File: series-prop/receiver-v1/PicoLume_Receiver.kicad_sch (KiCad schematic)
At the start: 67 parts, among them IC1 LM66200DRLR, J1 Conn_01x17, J10 Conn_01x03_Pin, J11 Conn_01x04_Pin, J13 USB_C_Receptacle_USB2.0_16P, J2 Conn_01x04_Pin, J4 Conn_01x17, J5 Conn_01x01_Pin, J6 Screw_Terminal_01x02, J7 Screw_Terminal_01x03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

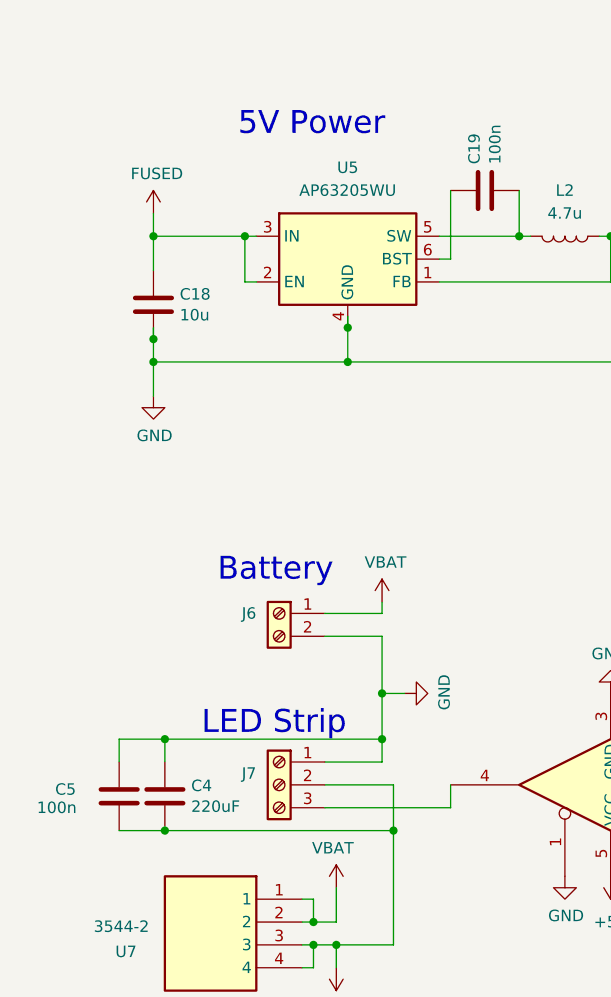
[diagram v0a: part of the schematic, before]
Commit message: Removed bulk output cap and added PTC on VBAT input
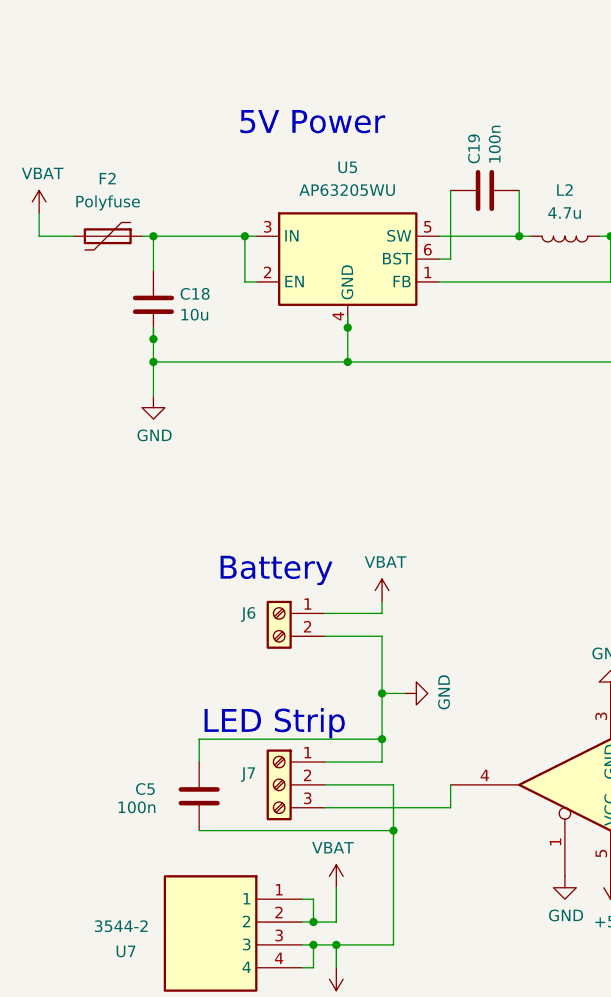
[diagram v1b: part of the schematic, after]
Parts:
- removed C4: 220uF, Capacitor_SMD:CP_Elec_8x10, symbol Device:C
- added F2: Polyfuse, Fuse:Fuse_1210_3225Metric, symbol Device:Polyfuse
- F1: footprint Fuse:Fuse_1206_3216Metric -> Fuse:Fuse_1210_3225Metric; LCSC C207036 -> C20617440
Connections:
- net FUSED: no longer C18.1, U5.2 (EN), U5.3 (IN)
- net VBAT: now also F2.2
- new net: C18.1, F2.1, U5.2 (EN), U5.3 (IN)
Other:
- moved on the sheet: C5
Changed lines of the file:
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@@
 	)
 	(junction
-		(at 49.53 177.8)
-		(diameter 0)
-		(color 0 0 0 0)
-	)
-	(junction
 		(at 88.9 111.76)
 		(diameter 0)
@@
 	)
 	(junction
-		(at 49.53 167.64)
-		(diameter 0)
-		(color 0 0 0 0)
-	)
-	(junction
 		(at 69.85 125.73)
 		(diameter 0)
@@
 	)
 	(junction
+		(at 48.26 111.76)
+		(diameter 0)
+		(color 0 0 0 0)
+	)
+	(junction
 		(at 73.66 59.69)
 		(diameter 0)
@@
 	)
 	(junction
-		(at 48.26 111.76)
-		(diameter 0)
-		(color 0 0 0 0)
-	)
-	(junction
 		(at 74.93 39.37)
 		(diameter 0)
@@
 	(wire
 		(pts
-			(xy 44.45 177.8) (xy 49.53 177.8)
-		)
-		(stroke
-			(width 0)
-			(type default)
-		)
-	)
-	(wire
-		(pts
 			(xy 201.93 109.22) (xy 201.93 114.3)
 		)
@@
 	(wire
 		(pts
+			(xy 35.56 111.76) (xy 39.37 111.76)
+		)
+		(stroke
+			(width 0)
+			(type default)
+		)
+	)
+	(wire
+		(pts
 			(xy 213.36 109.22) (xy 247.65 109.22)
 		)
@@
 	(wire
 		(pts
-			(xy 49.53 167.64) (xy 73.66 167.64)
+			(xy 53.34 167.64) (xy 73.66 167.64)
 		)
 		(stroke
@@
 	(wire
 		(pts
-			(xy 49.53 177.8) (xy 74.93 177.8)
+			(xy 53.34 177.8) (xy 74.93 177.8)
 		)
 		(stroke
@@
 	(wire
 		(pts
+			(xy 46.99 111.76) (xy 48.26 111.76)
+		)
+		(stroke
+			(width 0)
+			(type default)
+		)
+	)
+	(wire
+		(pts
 			(xy 373.38 36.83) (xy 387.35 36.83)
 		)
@@
 	(wire
 		(pts
-			(xy 49.53 167.64) (xy 49.53 170.18)
-		)
-		(stroke
-			(width 0)
-			(type default)
-		)
-	)
-	(wire
-		(pts
 			(xy 236.22 49.53) (xy 233.68 49.53)
 		)
@@
 	(wire
 		(pts
-			(xy 44.45 167.64) (xy 49.53 167.64)
-		)
-		(stroke
-			(width 0)
-			(type default)
-		)
-	)
-	(wire
-		(pts
 			(xy 279.4 105.41) (xy 290.83 105.41)
 		)
@@
 	(wire
 		(pts
+			(xy 35.56 109.22) (xy 35.56 111.76)
+		)
+		(stroke
+			(width 0)
+			(type default)
+		)
+	)
+	(wire
+		(pts
 			(xy 373.38 105.41) (xy 379.73 105.41)
 		)
@@
 	(wire
 		(pts
-			(xy 48.26 109.22) (xy 48.26 111.76)
-		)
-		(stroke
-			(width 0)
-			(type default)
-		)
-	)
-	(wire
-		(pts
 			(xy 379.73 33.02) (xy 379.73 34.29)
 		)
@@
 	(wire
 		(pts
-			(xy 44.45 170.18) (xy 44.45 167.64)
+			(xy 53.34 170.18) (xy 53.34 167.64)
 		)
 		(stroke
@@
 	(symbol
 		(lib_id "power:VBUS")
-		(at 48.26 109.22 0)
+		(at 35.56 109.22 0)
 		(unit 1)
 		(exclude_from_sim no)
@@
 		(dnp no)
 		(property "Reference" "#PWR047"
-			(at 48.26 113.03 0)
+			(at 35.56 113.03 0)
 			(effects
 				(font
@@
 			)
 		)
-		(property "Value" "FUSED"
-			(at 48.641 104.8258 0)
+		(property "Value" "VBAT"
+			(at 35.941 104.8258 0)
 			(effects
 				(font
@@
 		)
 		(property "Footprint" ""
-			(at 48.26 109.22 0)
+			(at 35.56 109.22 0)
 			(effects
 				(font
@@
 		)
 		(property "Datasheet" ""
-			(at 48.26 109.22 0)
+			(at 35.56 109.22 0)
 			(effects
 				(font
@@
 		)
 		(property "Description" "Power symbol creates a global label with name \"VBUS\""
-			(at 48.26 109.22 0)
+			(at 35.56 109.22 0)
 			(effects
 				(font
@@
 	(symbol
 		(lib_id "Device:C")
-		(at 49.53 173.99 0)
-		(unit 1)
-		(exclude_from_sim no)
-		(in_bom yes)
-		(on_board yes)
-		(dnp no)
-		(property "Reference" "C4"
-			(at 52.451 172.8216 0)
-			(effects
-				(font
-					(size 1.27 1.27)
-				)
-				(justify left)
-			)
-		)
-		(property "Value" "220uF"
-			(at 52.451 175.133 0)
-			(effects
-				(font
-					(size 1.27 1.27)
-				)
-				(justify left)
-			)
-		)
-		(property "Footprint" "Capacitor_SMD:CP_Elec_8x10"
-			(at 50.4952 177.8 0)
-			(effects
-				(font
-					(size 1.27 1.27)
-				)
-				(hide yes)
-			)
-		)
-		(property "Datasheet" "~"
-			(at 49.53 173.99 0)
-			(effects
-				(font
-					(size 1.27 1.27)
-				)
-				(hide yes)
-			)
-		)
-		(property "Description" "Unpolarized capacitor"
-			(at 49.53 173.99 0)
-			(effects
-				(font
-					(size 1.27 1.27)
-				)
-				(hide yes)
-			)
-		)
-		(property "LCSC" "C2164649"
-			(at 49.53 173.99 0)
-			(effects
-				(font
-					(size 1.27 1.27)
-				)
-				(hide yes)
-			)
-		)
-		(pin "1"
-		)
-		(pin "2"
-		)
-		(instances
-			(project "PicoLume_Receiver"
-				(path "/8c0b3d8b-46d3-4173-ab1e-a61765f77d61"
-					(reference "C4")
-					(unit 1)
-				)
-			)
-		)
-	)
-	(symbol
-		(lib_id "Device:C")
 		(at 111.76 118.11 0)
 		(unit 1)
@@
 			)
 		)
-		(property "Footprint" "Fuse:Fuse_1206_3216Metric"
+		(property "Footprint" "Fuse:Fuse_1210_3225Metric"
 			(at 77.47 38.1 0)
 			(effects
@@
 			)
 		)
-		(property "LCSC" "C207036"
+		(property "LCSC" "C20617440"
 			(at 82.55 36.83 90)
 			(effects
@@
 	)
 	(symbol
+		(lib_id "Device:Polyfuse")
+		(at 43.18 111.76 270)
+		(unit 1)
+		(exclude_from_sim no)
+		(in_bom yes)
+		(on_board yes)
+		(dnp no)
+		(fields_autoplaced yes)
+		(property "Reference" "F2"
+			(at 43.18 105.41 90)
+			(effects
+				(font
+					(size 1.27 1.27)
+				)
+			)
+		)
+		(property "Value" "Polyfuse"
+			(at 43.18 107.95 90)
+			(effects
+				(font
+					(size 1.27 1.27)
+				)
+			)
+		)
+		(property "Footprint" "Fuse:Fuse_1210_3225Metric"
+			(at 38.1 113.03 0)
+			(effects
+				(font
+					(size 1.27 1.27)
+				)
+				(justify left)
+				(hide yes)
+			)
+		)
+		(property "Datasheet" "~"
+			(at 43.18 111.76 0)
+			(effects
+				(font
+					(size 1.27 1.27)
+				)
+				(hide yes)
+			)
+		)
+		(property "Description" "Resettable fuse, polymeric positive temperature coefficient"
+			(at 43.18 111.76 0)
+			(effects
+				(font
+					(size 1.27 1.27)
+				)
+				(hide yes)
+			)
+		)
+		(property "LCSC" "C20617440"
+			(at 43.18 111.76 90)
+			(effects
+				(font
+					(size 1.27 1.27)
+				)
+				(hide yes)
+			)
+		)
+		(pin "1"
+		)
+		(pin "2"
+		)
+		(instances
+			(project "PicoLume_Receiver"
+				(path "/8c0b3d8b-46d3-4173-ab1e-a61765f77d61"
+					(reference "F2")
+					(unit 1)
+				)
+			)
+		)
+	)
+	(symbol
 		(lib_id "power:+3V3")
 		(at 379.73 107.95 270)
@@
 	(symbol
 		(lib_id "Device:C")
-		(at 44.45 173.99 0)
+		(at 53.34 173.99 0)
 		(unit 1)
 		(exclude_from_sim no)
@@
 		(dnp no)
 		(property "Reference" "C5"
-			(at 37.338 173.228 0)
+			(at 46.228 173.228 0)
 			(effects
 				(font
@@
 		)
 		(property "Value" "100n"
-			(at 35.306 175.26 0)
+			(at 44.196 175.26 0)
 			(effects
 				(font
@@
 		)
 		(property "Footprint" "Capacitor_SMD:C_0603_1608Metric"
-			(at 45.4152 177.8 0)
+			(at 54.3052 177.8 0)
 			(effects
 				(font
@@
 		)
 		(property "Datasheet" "~"
-			(at 44.45 173.99 0)
+			(at 53.34 173.99 0)
 			(effects
 				(font
@@
 		)
 		(property "Description" "Unpolarized capacitor"
-			(at 44.45 173.99 0)
+			(at 53.34 173.99 0)
 			(effects
 				(font
@@
 		)
 		(property "LCSC" "C14663"
-			(at 44.45 173.99 0)
+			(at 53.34 173.99 0)
 			(effects
 				(font

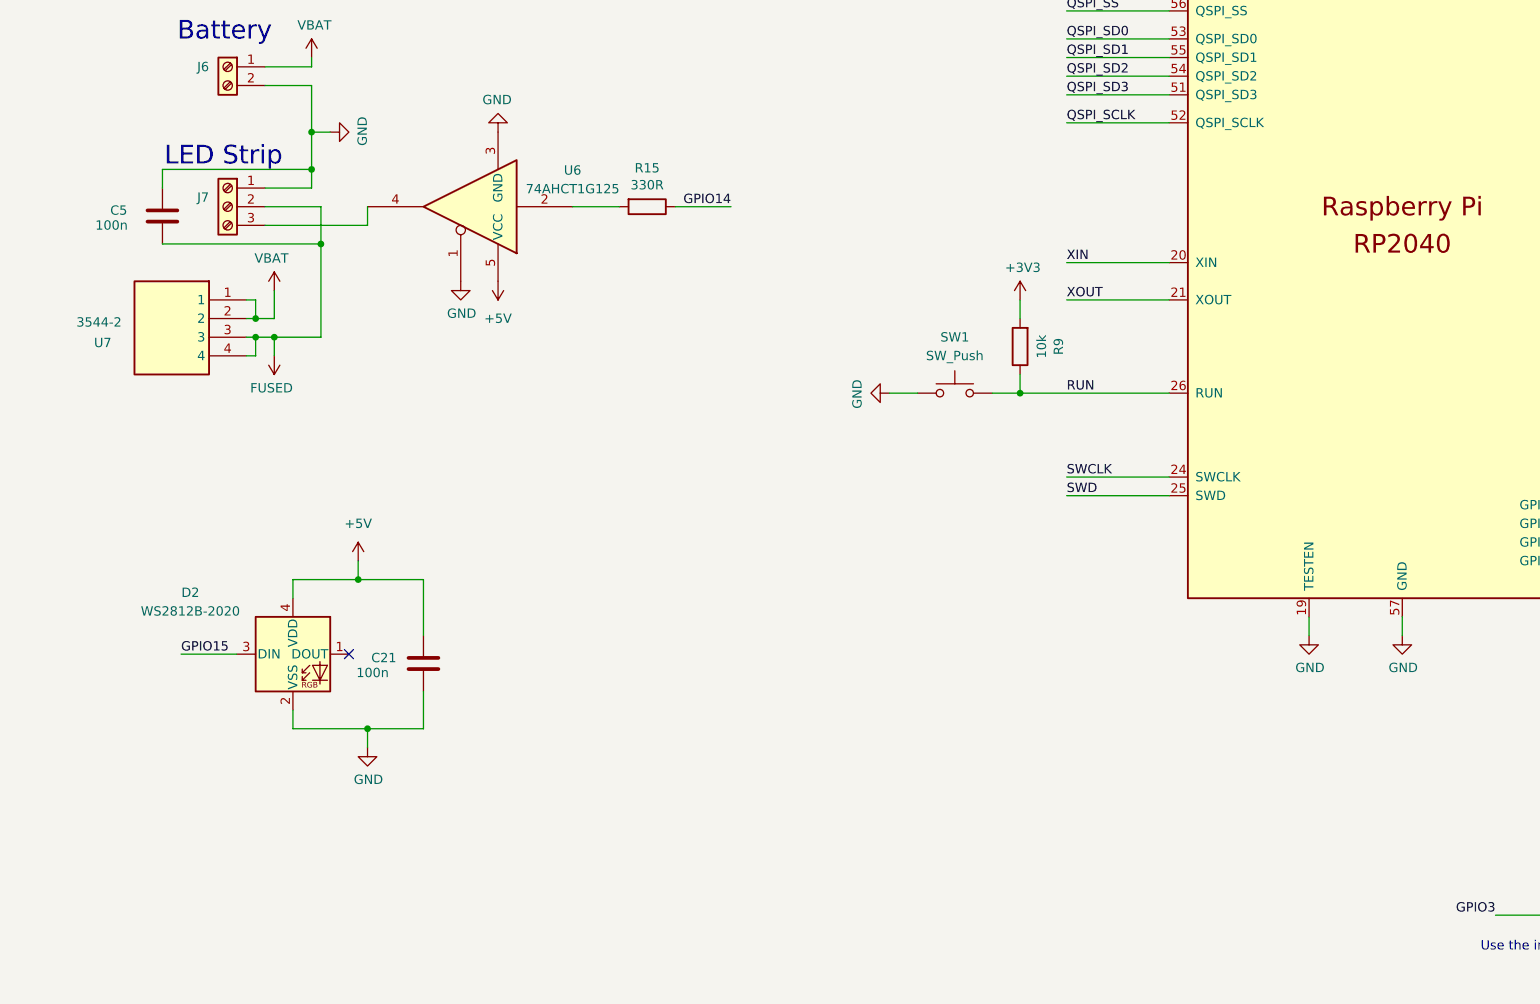
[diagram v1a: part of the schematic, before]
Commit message: replaced the RGB led with a button on GPIO15
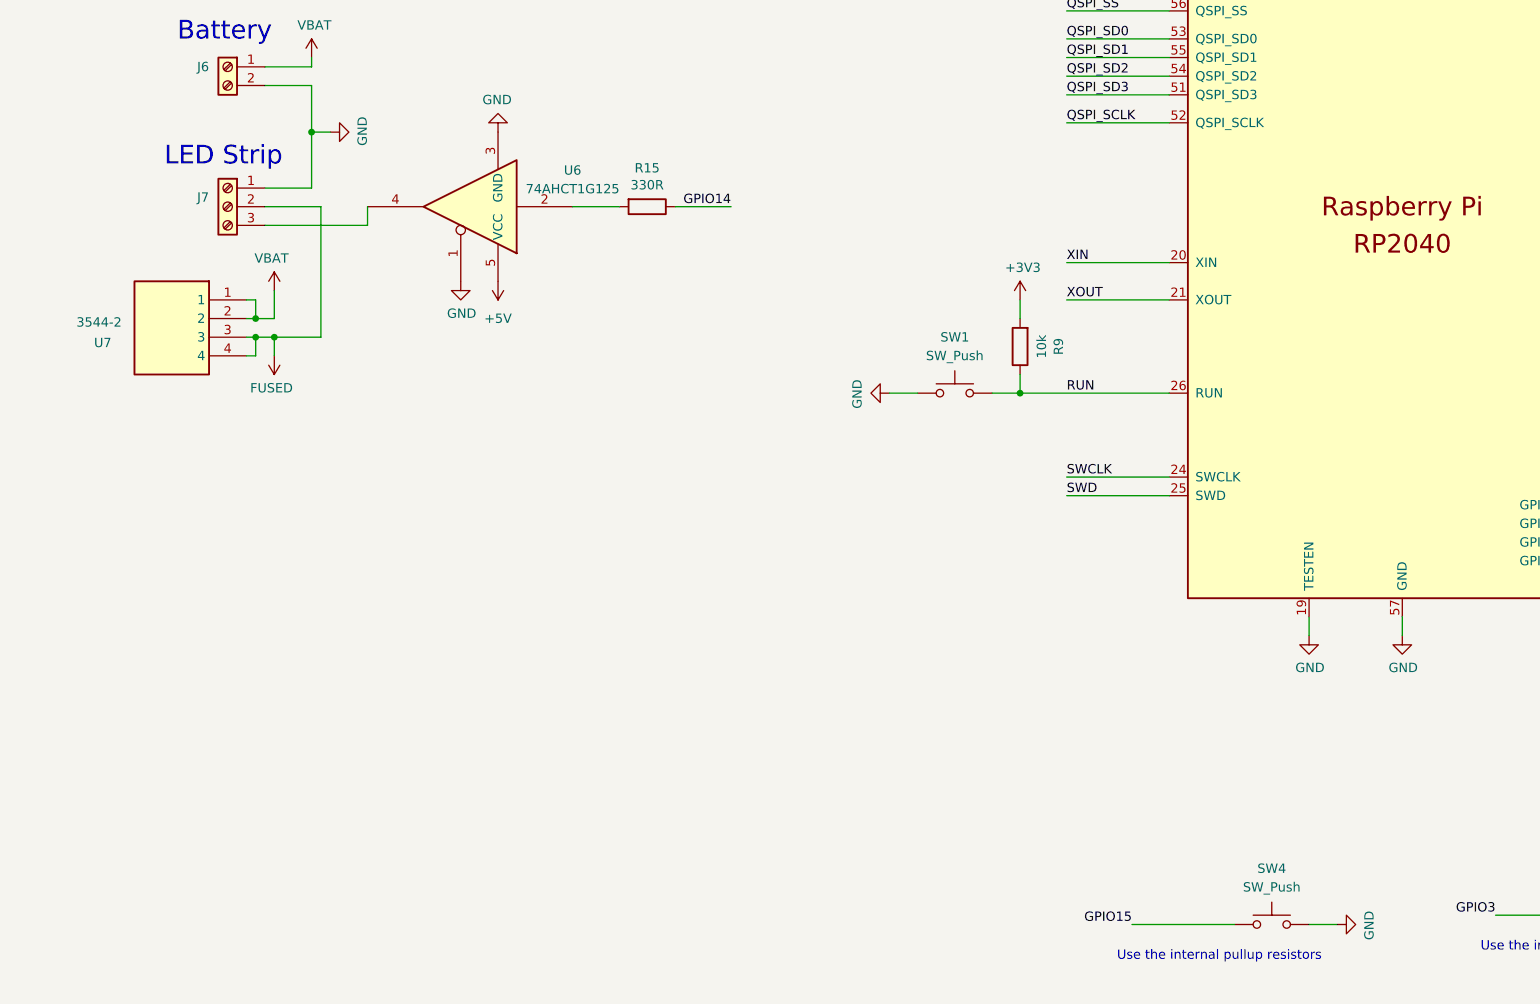
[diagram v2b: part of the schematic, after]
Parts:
- removed C21, C5: 100n, Capacitor_SMD:C_0603_1608Metric, symbol Device:C
- removed D2: WS2812B-2020, LED_SMD:LED_WS2812B-2020_PLCC4_2.0x2.0mm, symbol LED:WS2812B-2020
- added SW4: SW_Push, Button_Switch_SMD:SW_Tactile_SPST_NO_Straight_CK_PTS636Sx25SMTRLFS, symbol Switch:SW_Push
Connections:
- net GND: now also SW4.1
- net GPIO15: now also SW4.2
- no-connect marks 5 -> 4
